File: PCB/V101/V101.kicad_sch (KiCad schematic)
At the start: 0 parts

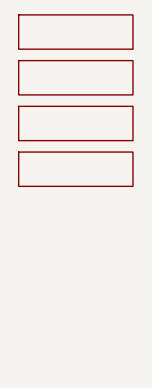
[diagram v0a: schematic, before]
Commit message: Updated PCB with PA & Block Diagram
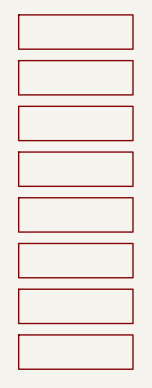
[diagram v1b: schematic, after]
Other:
- added sheet Interface-CANFD Sheet (Interface-CANFD.kicad_sch)
- added sheet Interface-RS485 (Interface-RS485.kicad_sch)
- added sheet Power (Power.kicad_sch)
- added sheet Sensors (Sensors.kicad_sch)
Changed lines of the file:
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@@
 	(paper "A4")
+	(sheet
+		(at 190.5 260.35)
+		(size 12.7 3.81)
+		(exclude_from_sim no)
+		(in_bom yes)
+		(on_board yes)
+		(dnp no)
+		(fields_autoplaced yes)
+		(stroke
+			(width 0.1524)
+			(type solid)
+		)
+		(fill
+			(color 0 0 0 0.0000)
+		)
+		(property "Sheetname" "Sensors"
+			(at 190.5 259.6384 0)
+			(effects
+				(font
+					(size 1.27 1.27)
+				)
+				(justify left bottom)
+				(hide yes)
+			)
+		)
+		(property "Sheetfile" "Sensors.kicad_sch"
+			(at 190.5 264.7446 0)
+			(effects
+				(font
+					(size 1.27 1.27)
+				)
+				(justify left top)
+				(hide yes)
+			)
+		)
+		(instances
+			(project "V101"
+				(path "/2bb6e42f-287e-4818-b6e1-26da2df0523c"
+					(page "7")
+				)
+			)
+		)
+	)
+	(sheet
+		(at 190.5 265.43)
+		(size 12.7 3.81)
+		(exclude_from_sim no)
+		(in_bom yes)
+		(on_board yes)
+		(dnp no)
+		(fields_autoplaced yes)
+		(stroke
+			(width 0.1524)
+			(type solid)
+		)
+		(fill
+			(color 0 0 0 0.0000)
+		)
+		(property "Sheetname" "Interface-RS485"
+			(at 190.5 264.7184 0)
+			(effects
+				(font
+					(size 1.27 1.27)
+				)
+				(justify left bottom)
+				(hide yes)
+			)
+		)
+		(property "Sheetfile" "Interface-RS485.kicad_sch"
+			(at 190.5 269.8246 0)
+			(effects
+				(font
+					(size 1.27 1.27)
+				)
+				(justify left top)
+				(hide yes)
+			)
+		)
+		(instances
+			(project "V101"
+				(path "/2bb6e42f-287e-4818-b6e1-26da2df0523c"
+					(page "8")
+				)
+			)
+		)
+	)
 	(sheet
 		(at 190.5 234.95)
@@
 				)
 			)
+		)
+	)
+	(sheet
+		(at 190.5 270.51)
+		(size 12.7 3.81)
+		(exclude_from_sim no)
+		(in_bom yes)
+		(on_board yes)
+		(dnp no)
+		(fields_autoplaced yes)
+		(stroke
+			(width 0.1524)
+			(type solid)
+		)
+		(fill
+			(color 0 0 0 0.0000)
+		)
+		(property "Sheetname" "Interface-CANFD Sheet"
+			(at 190.5 269.7984 0)
+			(effects
+				(font
+					(size 1.27 1.27)
+				)
+				(justify left bottom)
+				(hide yes)
+			)
+		)
+		(property "Sheetfile" "Interface-CANFD.kicad_sch"
+			(at 190.5 274.9046 0)
+			(effects
+				(font
+					(size 1.27 1.27)
+				)
+				(justify left top)
+				(hide yes)
+			)
+		)
+		(instances
+			(project "V101"
+				(path "/2bb6e42f-287e-4818-b6e1-26da2df0523c"
+					(page "9")
+				)
+			)
+		)
+	)
+	(sheet
+		(at 190.5 255.27)
+		(size 12.7 3.81)
+		(exclude_from_sim no)
+		(in_bom yes)
+		(on_board yes)
+		(dnp no)
+		(fields_autoplaced yes)
+		(stroke
+			(width 0.1524)
+			(type solid)
+		)
+		(fill
+			(color 0 0 0 0.0000)
+		)
+		(property "Sheetname" "Power"
+			(at 190.5 254.5584 0)
+			(effects
+				(font
+					(size 1.27 1.27)
+				)
+				(justify left bottom)
+				(hide yes)
+			)
+		)
+		(property "Sheetfile" "Power.kicad_sch"
+			(at 190.5 259.6646 0)
+			(effects
+				(font
+					(size 1.27 1.27)
+				)
+				(justify left top)
+				(hide yes)
+			)
+		)
+		(instances
+			(project "V101"
+				(path "/2bb6e42f-287e-4818-b6e1-26da2df0523c"
+					(page "6")
+				)
+			)

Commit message: Updated Layout
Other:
- added sheet Mechanical-Parts (Mechanical-Parts.kicad_sch)

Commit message: Updated PCB
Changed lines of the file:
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@@
 	(paper "A4")
 	(image
-		(at 146.05 87.63)
-		(scale 1.27656)
+		(at 149.86 88.9)
+		(scale 1.28967)
 		(data "/9j/4AAQSkZJRgABAQAAAQABAAD/2wBDAAgGBgcGBQgHBwcJCQgKDBQNDAsLDBkSEw8UHRofHh0a"
 			"HBwgJC4nICIsIxwcKDcpLDAxNDQ0Hyc5PTgyPC4zNDL/2wBDAQkJCQwLDBgNDRgyIRwhMjIyMjIy"
@@
 	)
 	(sheet
-		(at 190.5 260.35)
+		(at 289.56 180.34)
 		(size 12.7 3.81)
 		(exclude_from_sim no)
@@
 		)
 		(property "Sheetname" "Sensors"
-			(at 190.5 259.6384 0)
+			(at 289.56 179.6284 0)
 			(effects
 				(font
@@
 		)
 		(property "Sheetfile" "Sensors.kicad_sch"
-			(at 190.5 264.7446 0)
+			(at 289.56 184.7346 0)
 			(effects
 				(font
@@
 	)
 	(sheet
-		(at 190.5 265.43)
+		(at 289.56 185.42)
 		(size 12.7 3.81)
 		(exclude_from_sim no)
@@
 		)
 		(property "Sheetname" "Interface-RS485"
-			(at 190.5 264.7184 0)
+			(at 289.56 184.7084 0)
 			(effects
 				(font
@@
 		)
 		(property "Sheetfile" "Interface-RS485.kicad_sch"
-			(at 190.5 269.8246 0)
+			(at 289.56 189.8146 0)
 			(effects
 				(font
@@
 	)
 	(sheet
-		(at 190.5 275.59)
+		(at 289.56 195.58)
 		(size 12.7 3.81)
 		(exclude_from_sim no)
@@
 		)
 		(property "Sheetname" "Mechanical-Parts"
-			(at 190.5 274.8784 0)
+			(at 289.56 194.8684 0)
 			(effects
 				(font
@@
 		)
 		(property "Sheetfile" "Mechanical-Parts.kicad_sch"
-			(at 190.5 279.9846 0)
+			(at 289.56 199.9746 0)
 			(effects
 				(font
@@
 	)
 	(sheet
-		(at 190.5 234.95)
+		(at 289.56 154.94)
 		(size 12.7 3.81)
 		(exclude_from_sim no)
@@
 		)
 		(property "Sheetname" "Index"
-			(at 190.5 234.2384 0)
+			(at 289.56 154.2284 0)
 			(effects
 				(font
@@
 		)
 		(property "Sheetfile" "Index.kicad_sch"
-			(at 190.5 239.3446 0)
+			(at 289.56 159.3346 0)
 			(effects
 				(font
@@
 	)
 	(sheet
-		(at 190.5 240.03)
+		(at 289.56 160.02)
 		(size 12.7 3.81)
 		(exclude_from_sim no)
@@
 		)
 		(property "Sheetname" "Block_Diagram"
-			(at 190.5 239.3184 0)
+			(at 289.56 159.3084 0)
 			(effects
 				(font
@@
 		)
 		(property "Sheetfile" "Block_Diagram.kicad_sch"
-			(at 190.5 244.4246 0)
+			(at 289.56 164.4146 0)
 			(effects
 				(font
@@
 	)
 	(sheet
-		(at 190.5 250.19)
+		(at 289.56 170.18)
 		(size 12.7 3.81)
 		(exclude_from_sim no)
@@
 		)
 		(property "Sheetname" "MCU"
-			(at 190.5 249.4784 0)
+			(at 289.56 169.4684 0)
 			(effects
 				(font
@@
 		)
 		(property "Sheetfile" "MCU.kicad_sch"
-			(at 190.5 254.5846 0)
+			(at 289.56 174.5746 0)
 			(effects
 				(font
@@
 	)
 	(sheet
-		(at 190.5 245.11)
+		(at 289.56 165.1)
 		(size 12.7 3.81)
 		(exclude_from_sim no)
@@
 		)
 		(property "Sheetname" "Project_Architecture"
-			(at 190.5 244.3984 0)
+			(at 289.56 164.3884 0)
 			(effects
 				(font
@@
 		)
 		(property "Sheetfile" "Project_Architecture.kicad_sch"
-			(at 190.5 249.5046 0)
+			(at 289.56 169.4946 0)
 			(effects
 				(font
@@
 	)
 	(sheet
-		(at 190.5 270.51)
+		(at 289.56 190.5)
 		(size 12.7 3.81)
 		(exclude_from_sim no)
@@
 		)
 		(property "Sheetname" "Interface-CANFD Sheet"
-			(at 190.5 269.7984 0)
+			(at 289.56 189.7884 0)
 			(effects
 				(font
@@
 		)
 		(property "Sheetfile" "Interface-CANFD.kicad_sch"
-			(at 190.5 274.9046 0)
+			(at 289.56 194.8946 0)
 			(effects
 				(font
@@
 	)
 	(sheet
-		(at 190.5 255.27)
+		(at 289.56 175.26)
 		(size 12.7 3.81)
 		(exclude_from_sim no)
@@
 		)
 		(property "Sheetname" "Power"
-			(at 190.5 254.5584 0)
+			(at 289.56 174.5484 0)
 			(effects
 				(font
@@
 		)
 		(property "Sheetfile" "Power.kicad_sch"
-			(at 190.5 259.6646 0)
+			(at 289.56 179.6546 0)
 			(effects
 				(font
